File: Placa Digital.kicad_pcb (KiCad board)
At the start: 2 copper layers, 60 x 80 mm, 23 parts, among them J1 Entradas / Salidas, Q1 BC548, Q2 BC548, U1 EC11_Module, U2 Alimentación, U3 ST7920_Display, U4 10K

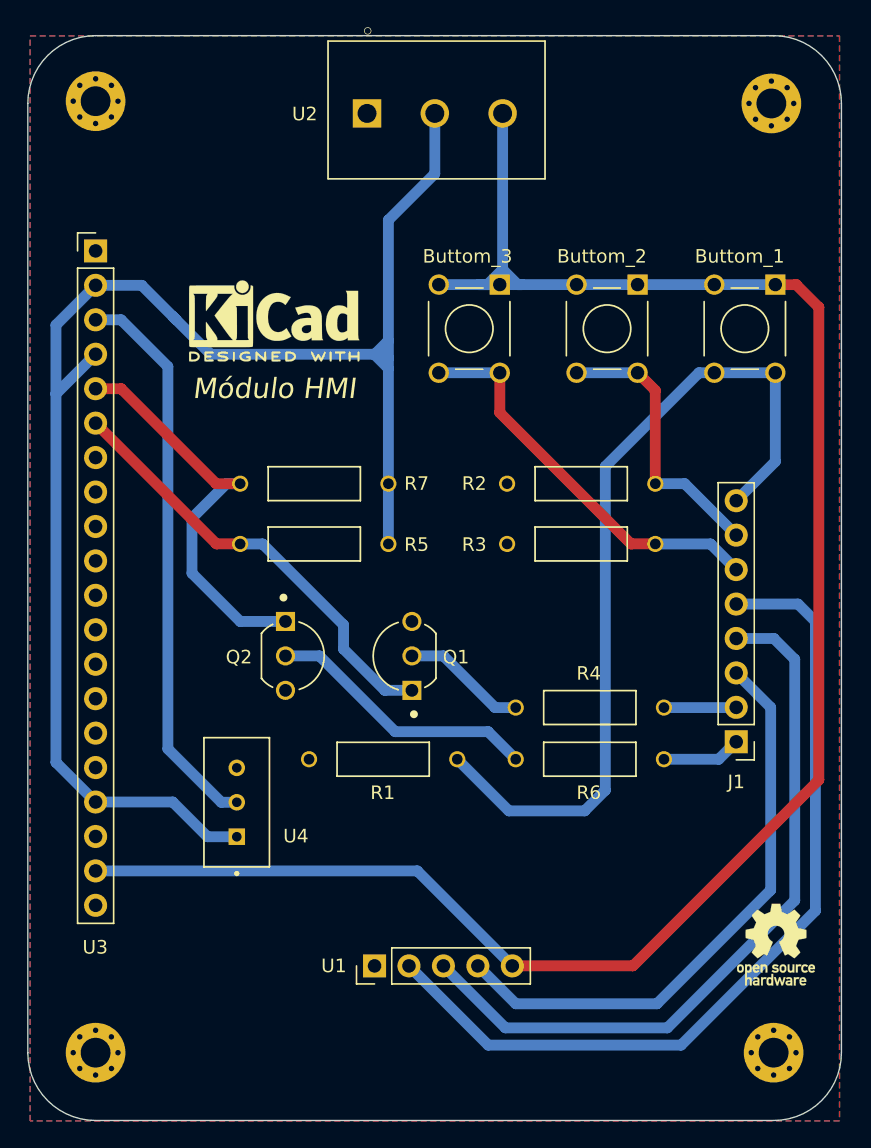
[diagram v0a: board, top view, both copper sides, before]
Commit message: Added 3d model + 1 Layer
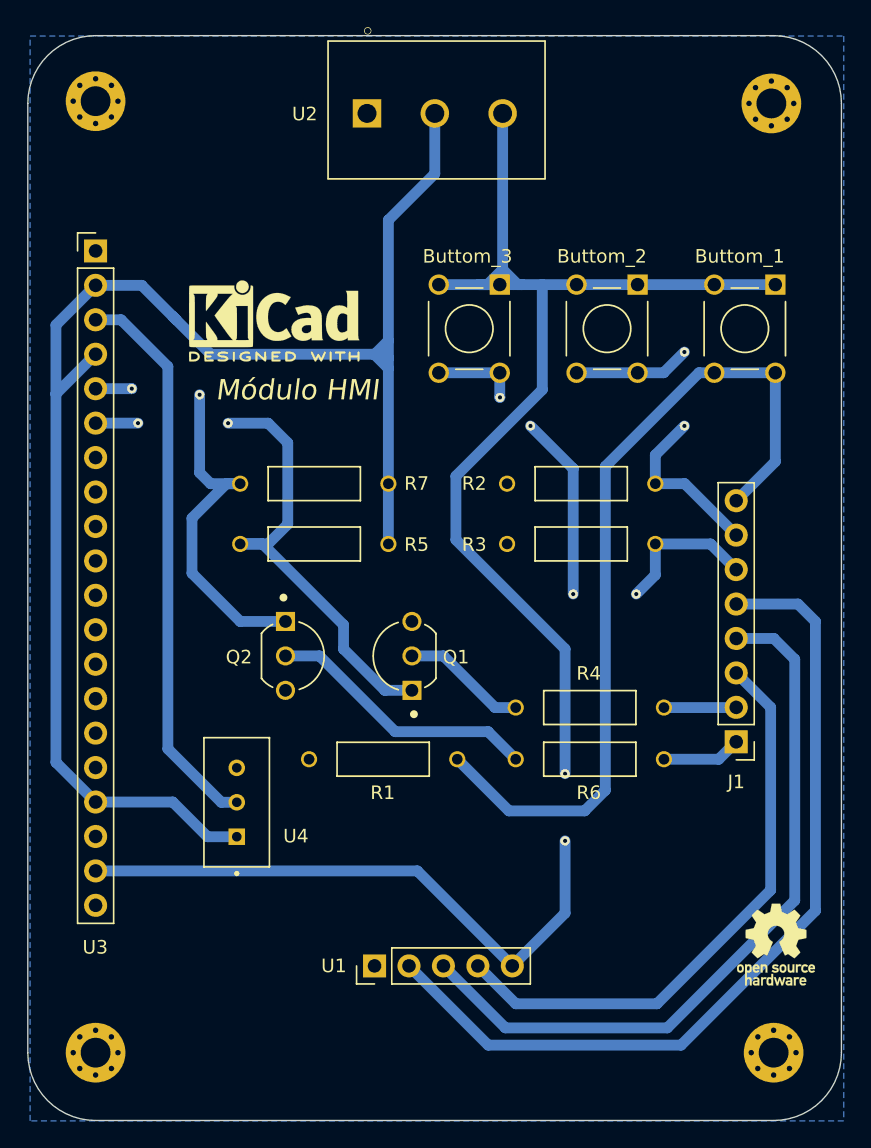
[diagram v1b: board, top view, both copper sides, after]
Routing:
- net +3V3: track 145.8 -> 131.6 mm, vias 0 -> 2
- net Net-(Q1-Pad1): track 32.5 -> 36.4 mm, vias 0 -> 2
- net Net-(Q2-Pad1): track 30.6 -> 28.8 mm, vias 0 -> 2
- net /toMicroC_Button3: track 29.7 -> 31.1 mm, vias 0 -> 4
- net /toMicroC_Button2: track 20.8 -> 21.3 mm, vias 0 -> 2
- removed copper zone on F.Cu, net GND
